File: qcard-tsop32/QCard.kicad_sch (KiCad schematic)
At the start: 4 parts, among them J1 Conn_02x18_Top_Bottom, U1 SST39SF040

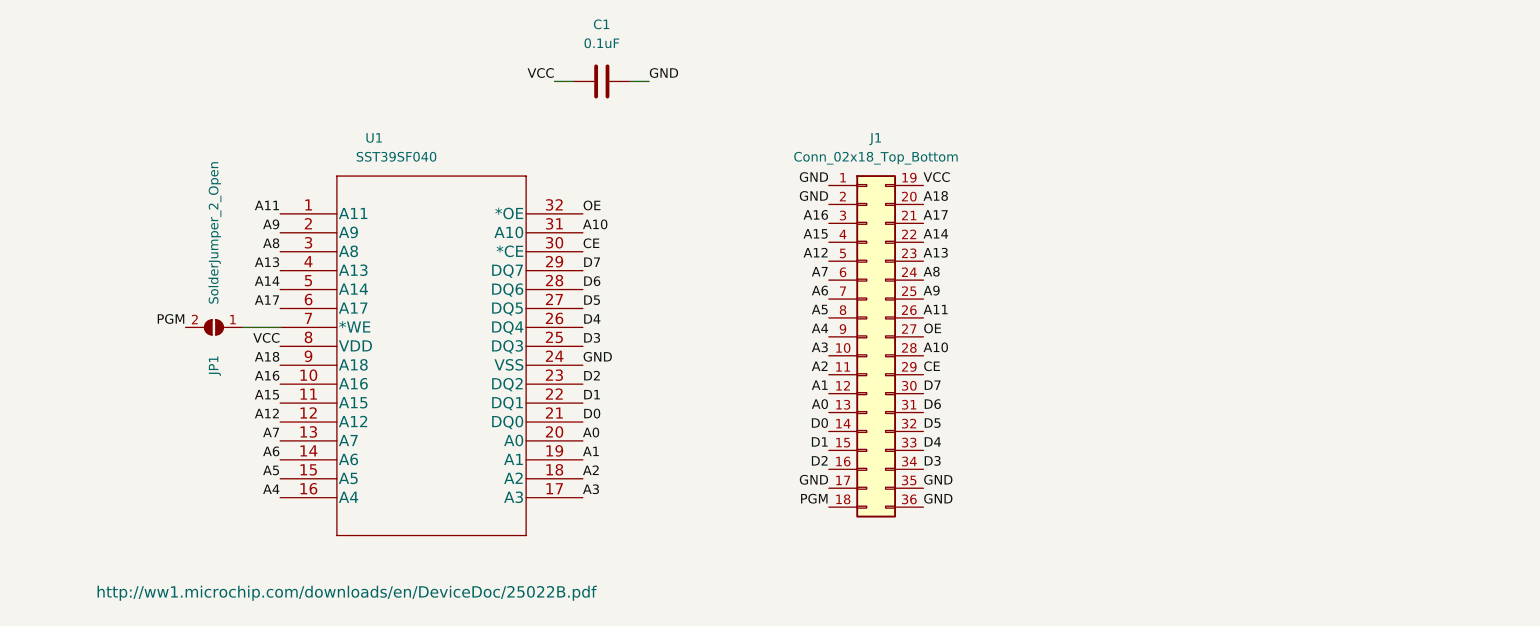
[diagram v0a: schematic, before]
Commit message: Better write protect jumper behaviour, using text vars
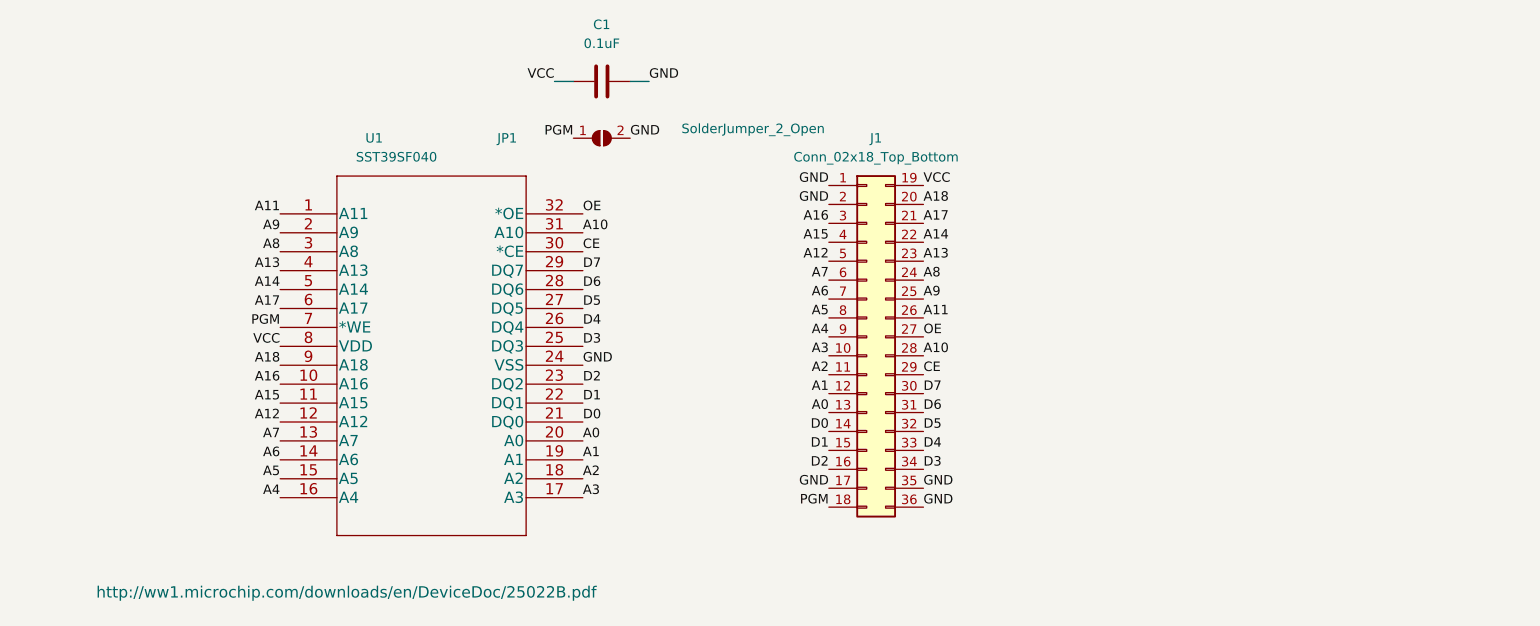
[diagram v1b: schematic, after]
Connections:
- net GND: now also JP1.2 (B)
- net PGM: now also JP1.1 (A), U1.7 (*WE); no longer JP1.2 (B)
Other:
- moved on the sheet: JP1
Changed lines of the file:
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@@
     (stroke (width 0) (type default) (color 0 0 0 0))
   )
-  (wire (pts (xy 31.75 60.96) (xy 36.83 60.96))
-    (stroke (width 0) (type default) (color 0 0 0 0))
-  )
   (label "A0" (at 110.49 72.39 180)
     (effects (font (size 1.27 1.27)) (justify right bottom))
@@
     (effects (font (size 1.27 1.27)) (justify left bottom))
   )
+  (label "GND" (at 83.82 35.56 0)
+    (effects (font (size 1.27 1.27)) (justify left bottom))
+  )
   (label "VCC" (at 123.19 41.91 0)
     (effects (font (size 1.27 1.27)) (justify left bottom))
@@
     (effects (font (size 1.27 1.27)) (justify left bottom))
   )
+  (label "PGM" (at 36.83 60.96 180)
+    (effects (font (size 1.27 1.27)) (justify right bottom))
+  )
   (label "A7" (at 36.83 76.2 180)
     (effects (font (size 1.27 1.27)) (justify right bottom))
@@
     (effects (font (size 1.27 1.27)) (justify right bottom))
   )
-  (label "PGM" (at 24.13 60.96 180)
+  (label "PGM" (at 76.2 35.56 180)
     (effects (font (size 1.27 1.27)) (justify right bottom))
   )
@@
     (pin "2")
   )
-  (symbol (lib_id "Jumper:SolderJumper_2_Open") (at 27.94 60.96 180) (unit 1)
+  (symbol (lib_id "Jumper:SolderJumper_2_Open") (at 80.01 35.56 0) (unit 1)
     (in_bom yes) (on_board yes)
-    (property "Reference" "JP1" (id 0) (at 27.94 66.04 90))
-    (property "Value" "SolderJumper_2_Open" (id 1) (at 27.94 48.26 90))
-    (property "Footprint" "Jumper:SolderJumper-2_P1.3mm_Open_RoundedPad1.0x1.5mm" (id 2) (at 27.94 60.96 0)
-      (effects (font (size 1.27 1.27)) hide)
-    )
-    (property "Datasheet" "~" (id 3) (at 27.94 60.96 0)
-      (effects (font (size 1.27 1.27)) hide)
-    )
+    (property "Reference" "JP1" (id 0) (at 67.31 35.56 0))
+    (property "Value" "SolderJumper_2_Open" (id 1) (at 100.33 34.29 0))
+    (property "Footprint" "Jumper:SolderJumper-2_P1.3mm_Open_RoundedPad1.0x1.5mm" (id 2) (at 80.01 35.56 0)
+      (effects (font (size 1.27 1.27)) hide)
+    )
+    (property "Datasheet" "~" (id 3) (at 80.01 35.56 0)
+      (effects (font (size 1.27 1.27)) hide)
+    )

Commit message: Solve ERC warnings
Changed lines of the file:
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@@
 (kicad_sch (version 20211123) (generator eeschema)
   (paper "A4")
-  (wire (pts (xy 83.82 27.94) (xy 86.36 27.94))
+  (junction (at 88.9 27.94) (diameter 0) (color 0 0 0 0)
+  )
+  (junction (at 72.39 27.94) (diameter 0) (color 0 0 0 0)
+  )
+  (wire (pts (xy 72.39 27.94) (xy 76.2 27.94))
     (stroke (width 0) (type default) (color 0 0 0 0))
   )
-  (wire (pts (xy 73.66 27.94) (xy 76.2 27.94))
+  (wire (pts (xy 83.82 27.94) (xy 88.9 27.94))
     (stroke (width 0) (type default) (color 0 0 0 0))
   )
+  (wire (pts (xy 67.31 27.94) (xy 72.39 27.94))
+    (stroke (width 0) (type default) (color 0 0 0 0))
+  )
+  (wire (pts (xy 88.9 27.94) (xy 93.98 27.94))
+    (stroke (width 0) (type default) (color 0 0 0 0))
+  )
   (label "A0" (at 110.49 72.39 180)
     (effects (font (size 1.27 1.27)) (justify right bottom))
@@
     (effects (font (size 1.27 1.27)) (justify left bottom))
   )
-  (label "GND" (at 86.36 27.94 0)
+  (label "GND" (at 93.98 27.94 0)
     (effects (font (size 1.27 1.27)) (justify left bottom))
   )
@@
     (effects (font (size 1.27 1.27)) (justify right bottom))
   )
-  (label "VCC" (at 73.66 27.94 180)
+  (label "VCC" (at 67.31 27.94 180)
     (effects (font (size 1.27 1.27)) (justify right bottom))
   )
@@
     (pin "1")
     (pin "2")
+  )
+  (symbol (lib_id "power:PWR_FLAG") (at 88.9 27.94 0) (mirror y) (unit 1)
+    (in_bom yes) (on_board yes) (fields_autoplaced)
+    (property "Reference" "#FLG0101" (id 0) (at 88.9 26.035 0)
+      (effects (font (size 1.27 1.27)) hide)
+    )
+    (property "Value" "PWR_FLAG" (id 1) (at 88.9 22.86 0))
+    (property "Footprint" "" (id 2) (at 88.9 27.94 0)
+      (effects (font (size 1.27 1.27)) hide)
+    )
+    (property "Datasheet" "~" (id 3) (at 88.9 27.94 0)
+      (effects (font (size 1.27 1.27)) hide)
+    )
+    (pin "1")
   )
   (symbol (lib_id "Connector_Generic:Conn_02x18_Top_Bottom") (at 115.57 62.23 0) (unit 1)
@@
     (pin "9")
   )
+  (symbol (lib_id "power:PWR_FLAG") (at 72.39 27.94 0) (mirror y) (unit 1)
+    (in_bom yes) (on_board yes) (fields_autoplaced)
+    (property "Reference" "#FLG0102" (id 0) (at 72.39 26.035 0)
+      (effects (font (size 1.27 1.27)) hide)
+    )
+    (property "Value" "PWR_FLAG" (id 1) (at 72.39 22.86 0))
+    (property "Footprint" "" (id 2) (at 72.39 27.94 0)
+      (effects (font (size 1.27 1.27)) hide)
+    )
+    (property "Datasheet" "~" (id 3) (at 72.39 27.94 0)
+      (effects (font (size 1.27 1.27)) hide)
+    )
+    (pin "1")
+  )
   (sheet_instances
     (path "/" (page "1"))
   )
   (symbol_instances
+    (path "/90a95fdd-b294-4b30-a4da-cb414ca2a87d"
+      (reference "#FLG0101") (unit 1) (value "PWR_FLAG") (footprint "")
+    )
+    (path "/e1fe7c8c-97aa-4319-a20b-1d632e336249"
+      (reference "#FLG0102") (unit 1) (value "PWR_FLAG") (footprint "")
+    )
     (path "/4d71f0ca-fe25-41a1-8dcd-28e56c5e269f"
       (reference "C1") (unit 1) (value "0.1uF") (footprint "Capacitor_SMD:C_0805_2012Metric_Pad1.18x1.45mm_HandSolder")

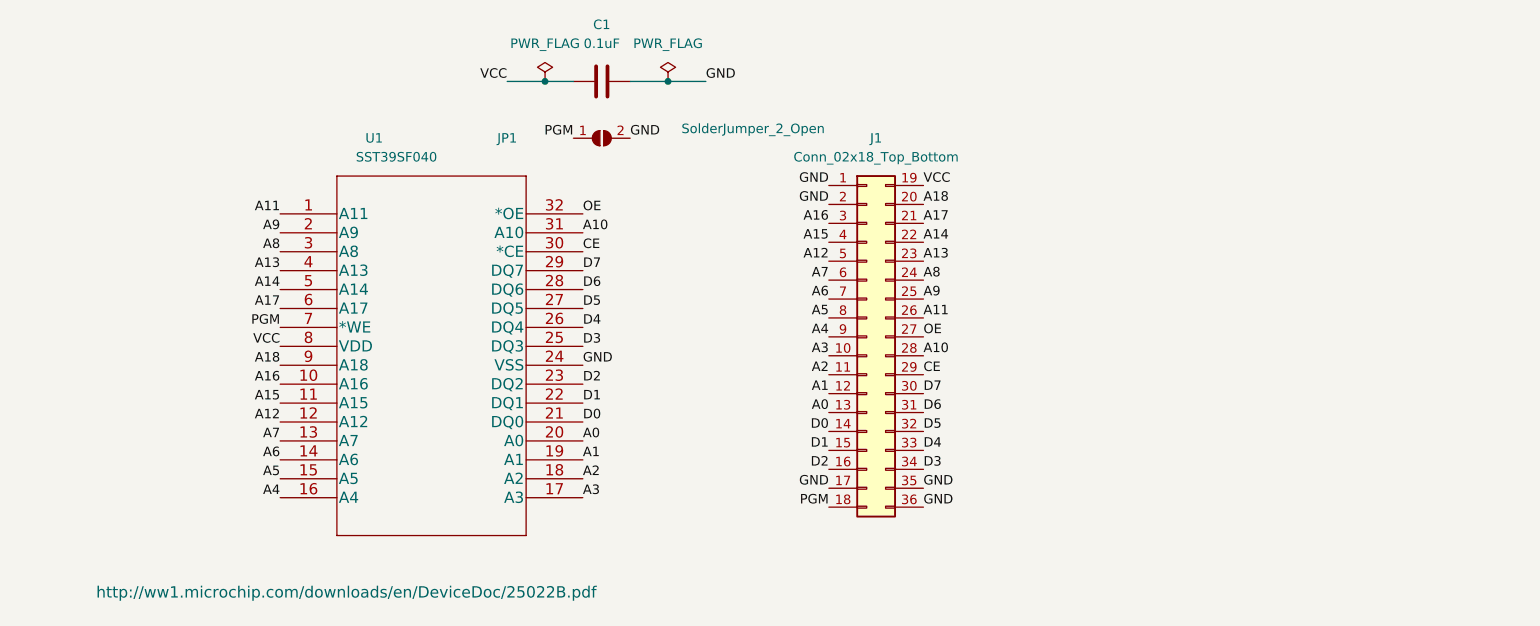
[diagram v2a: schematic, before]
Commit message: Pulling WE high for reading per datasheet
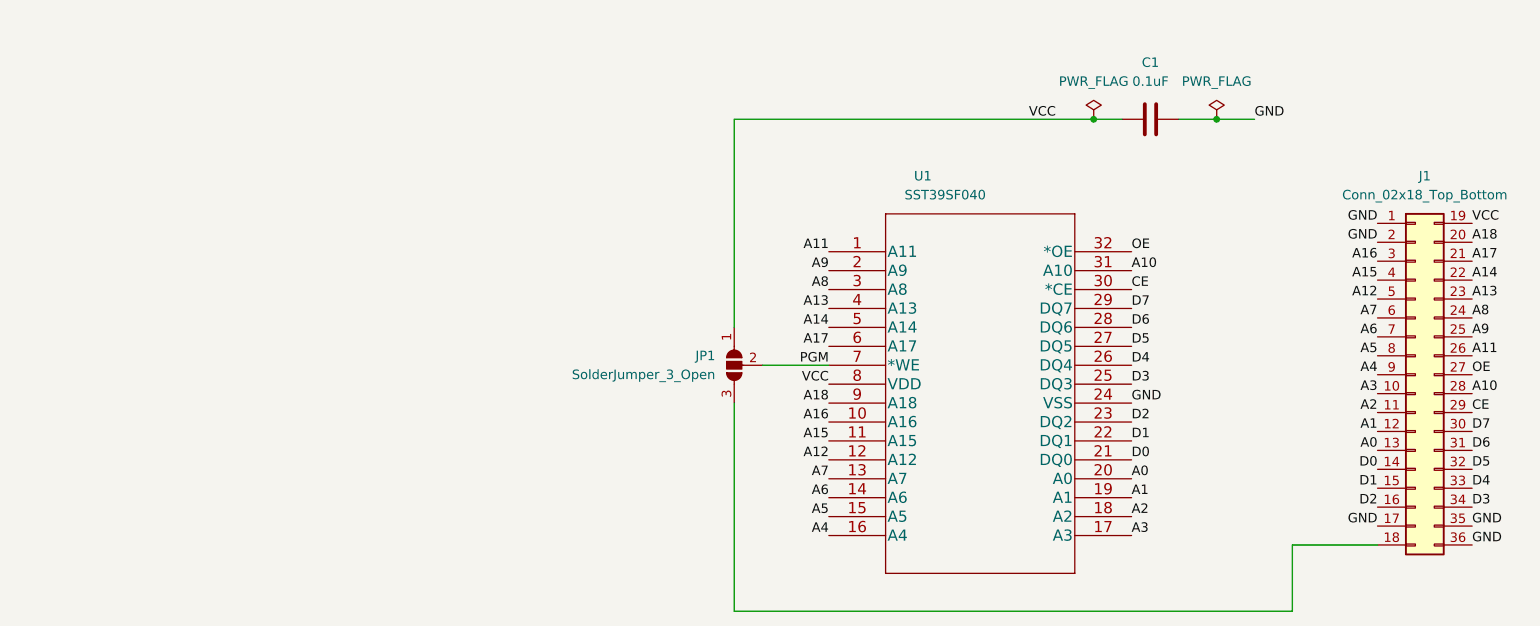
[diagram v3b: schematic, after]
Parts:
- removed JP1: SolderJumper_2_Open, Jumper:SolderJumper-2_P1.3mm_Open_RoundedPad1.0x1.5mm, symbol Jumper:SolderJumper_2_Open
- added JP1: SolderJumper_3_Open, Jumper:SolderJumper-3_P1.3mm_Open_Pad1.0x1.5mm, symbol Jumper:SolderJumper_3_Open
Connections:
- net PGM: now also JP1.2 (C); no longer J1.18 (Pin_18)
- net VCC: now also JP1.1 (A)
- new net: J1.18 (Pin_18), JP1.3 (B)
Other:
- moved on the sheet: C1, J1, U1
